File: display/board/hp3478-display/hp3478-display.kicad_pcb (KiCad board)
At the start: 2 copper layers, 130.2 x 30.2 mm, 4 parts, among them U1 PIC16F152xx-x_MP, U2 PIC16F152xx-x_PT

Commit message: Clean up DNP alternate footprint for PIC.
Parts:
- U1: value PIC16F152xx-x_MP -> PIC16F15274-I/MP
- U2: value PIC16F152xx-x_PT -> DNP
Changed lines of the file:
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@@
       (effects (font (size 1 1) (thickness 0.15)) (justify mirror))
     )
-    (fp_text value "PIC16F152xx-x_MP" (at 0 -3.82) (layer "B.Fab")
+    (fp_text value "PIC16F15274-I/MP" (at 0 -3.46875) (layer "B.Fab")
       (effects (font (size 1 1) (thickness 0.15)) (justify mirror))
     )
@@
     (property "Sheetfile" "hp3478-display.kicad_sch")
     (property "Sheetname" "")
-    (attr smd)
+    (property "exclude_from_bom" "")
+    (attr smd exclude_from_pos_files exclude_from_bom)
     (fp_text reference "U2" (at 0 7.45) (layer "B.SilkS") hide
       (effects (font (size 1 1) (thickness 0.15)) (justify mirror))
     )
-    (fp_text value "PIC16F152xx-x_PT" (at 0 -7.45) (layer "B.Fab")
+    (fp_text value "DNP" (at 0 -5.86875) (layer "B.Fab")
       (effects (font (size 1 1) (thickness 0.15)) (justify mirror))
     )
-    (fp_text user "${REFERENCE}" (at 0 0) (layer "B.Fab")
+    (fp_text user "${REFERENCE}" (at 0 4.13125) (layer "B.Fab")
       (effects (font (size 1 1) (thickness 0.15)) (justify mirror))
     )
@@
     )
   )
+  (group "" (id 6e3d8511-2586-4d9e-937b-9cb906607ab9)
+    (members
+      025682ff-41e6-48d6-90bc-8bc9fd15746c
+      0283738d-a418-4d7b-9e19-75ddbebbf050
+      06bb3c45-8662-472c-9176-38043edc8433
+      08d35165-bb31-44e7-9429-80a805175552
+      0a7519a3-5bb3-4d21-a876-66e5dc7dcb8d
+      0e3858fa-84b2-4190-b5dc-bcf350b77c61
+      101c4e56-94ee-448a-ae09-c0221e6f2d51
+      145eaf54-18e0-4b79-ba03-246c116e8f69
+      15e94442-0598-4a45-91b8-03f9b70ef5a3
+      16da12bf-2bc4-4194-ac8b-406fff70d2c3
+      1715dd60-2482-4e23-bc5e-3ba31d700b6f
+      1890f8e7-7f4d-463f-aff9-8671ab63580d
+      192e3839-8763-4b24-a518-5f7d4922fde5
+      1a80f237-de71-4763-80b9-d5010554198d
+      1c2f6f5d-567d-492e-90b1-d03751b21de6
+      1e06e057-1898-481f-9c88-3f5ebfa1e2fc
+      2028c6f6-e3dc-4ebc-aa0a-1362c4c273f7
+      21570638-80d9-4bae-a6cb-664d093151eb
+      2b77d2c8-977c-4773-b0bd-bde5d2c77fbc
+      2c354cff-9b07-49b8-ba75-7a25afc01f8d
+      2d844d1e-d000-4622-833b-a95b405f524e
+      2f1c99e4-9708-4779-a084-75db109c2f9c
+      2ffade97-e93c-4eaa-aabd-0226b2760495
+      345a010e-1fef-4904-91f1-bda43f6b94d0
+      34ce5afb-6d00-4f5b-96d5-474654a69470
+      37c44871-b5ca-4b38-aea3-1001c85da830
+      38ca2c34-44e4-4c73-9ecb-227d72018ede
+      4341d2f5-8f69-4bb4-89b6-485b5ccc8d94
+      48f444ee-de87-45be-b1f9-c20f4807963d
+      4db15927-cf44-4c49-9d54-4b4de7338f36
+      4eb2b707-4e67-4a79-8fa4-d5b3344d5c35
+      500f0cbe-700d-4821-bc8f-60759eeacedf
+      50c01e0b-0ee6-472b-9333-2379db306fa4
+      522140c8-51df-4cb0-80d1-d66afb59c4b8
+      530f5c91-5b5c-418c-b140-c1ccb08f07bb
+      54c19f1b-d006-4448-b08e-ed09ffd527e8
+      5bf72b43-8bfb-4f08-808e-46a6203671c8
+      5c8c4710-eed1-4240-878e-82181da0927d
+      5d507657-9866-419e-8279-080b059aeacd
+      5fac6f2c-6c6b-43ac-8c10-2c6f79dc15c3
+      60ea5389-bad7-4455-8498-5ab0665097fa
+      6580a8f1-f2ac-4be7-a759-ec333c75ea6f
+      67b13574-aef6-4e34-a5da-0348eaf75eff
+      683e9974-205a-4b76-84d5-c61235e00cdf
+      69365ee1-a7b1-43a5-8bad-a7db095cd6be
+      6c9397ea-235b-4ac5-ae90-efeac14b9162
+      7453fe99-c82a-4f4c-a960-c47a3c9abc0f
+      7adde682-d9cf-422d-8b9e-de7041a547f6
+      7b3583d4-0dcd-478a-9b70-53631796ddab
+      7b6b4f66-b8ef-4714-8f97-ea658228ba10
+      7d41948f-1b4b-4190-b337-199c340481b0
+      7d8cd68e-53e9-4780-a7b5-81e893b4aa44
+      7f1df24b-7067-45e9-8d0d-c04f6979bd1a
+      80d0327f-3161-4396-8853-6ca9f9deef36
+      81a76000-c235-495d-badf-e67f0e22323d
+      820e6614-d287-4578-9e51-4bf87f4b5f3c
+      82da71be-ab20-4e92-88af-ef4b842e5e4d
+      830267ac-4842-41eb-85aa-0bdeaf4c5da1
+      83f673a8-bf08-4bb5-a175-211bee14410e
+      83f68b42-ad69-4a08-a66f-0f1ad597741f
+      8976d532-97e7-4390-a5ee-ff48eeba3bc3
+      8d60349a-2b6c-4737-b106-263838d93f65
+      8f6142be-d54e-4d35-94e1-84ddd3d928f6
+      8f89d360-3807-4139-b3b1-4daea565fc2c
+      905a91b7-0f34-44b1-a98b-4c84c5d3c34e
+      93c134d8-7f21-4c40-8af1-1590fcb8ea30
+      9693fdcf-ada8-4fa4-902a-d7bcc7cb52e6
+      9ac5a0d4-3a85-4749-8d01-72dc6705821e
+      9e2301b9-18b8-493f-b249-928001b48921
+      9e802228-d3ca-450d-b5c2-e1e0526f26b0
+      9f70f681-a65d-4bfe-9163-cd3986453b6a
+      a2651f45-f233-4f7f-891c-41cf7e834619
+      a51fe366-2aae-45c2-aff7-f7f2d42fdd5c
+      acfde106-6ae1-4e80-ad04-4b11c2077337
+      ad824e11-9e43-4081-a47a-41356cebcfa1
+      ad8984a6-46a2-46bf-b149-408e18283ee8
+      ada6ff82-316c-40eb-ac3b-dee42e3d0fe0
+      adebfdb4-2d29-4cab-bad6-861392e3a973
+      aea8aee0-6918-4849-8951-0758496f3f77
+      af461771-7716-49bc-b6e1-a0cd07300201
+      b04d9136-b36c-4fd5-81bf-de6d48d242fd
+      b26fcc2b-fcf2-4a0d-bd8e-73c5c37df574
+      b2df7048-676f-4e9f-a937-85724a31c4da
+      b30e7e2d-9e8f-427b-b3de-40406137f752
+      b6e7d491-e815-46fe-a70b-e4e69542d985
+      b7a6e4bf-85bd-459a-8fae-cc24559051f6
+      bae503f5-737d-431e-ad8e-a732e1761b1b
+      bb3598e4-5f7d-4578-8eaf-08a0b2819f65
+      bba42b20-991e-4b6c-94ce-3b8912e848cc
+      bcafb699-73d4-48c1-8afc-c47ad2e6a319
+      bdda3f47-5fbc-4808-9d0b-3855365750ce
+      bf88b221-8c08-490d-8b1e-a107943edec0
+      c29e7f6c-6f8d-4f9c-973a-28026f9df1fb
+      c3786e45-6ed3-4e76-b21e-8784af082722
+      c50321ff-67fb-48a0-8459-fb8f04cc8330
+      c54809be-ddf7-4216-9bbe-d9ddd9bf1732
+      c5be51fb-343e-4a7f-b84b-60e8d21d866d
+      c9b8864b-ae54-495f-b221-7e6ec6c709a7
+      c9c9879b-016f-4837-ba81-059978bb2217
+      cae04ccc-ad7f-4d0e-bf06-386c7f95600e
+      cb28fc78-1799-48b6-b37d-a09e1e163ce1
+      cc302e30-08b3-40db-aea0-b70b83d47abb
+      cdaa8dca-88ad-4603-92ae-986a07685d3f
+      ce3cb9d7-7434-4c77-b49b-2743514ac2a5
+      d159ef80-b12c-4e4a-aac0-afe11b2aec94
+      d29bf029-20ec-498e-be4e-c731095d4b1c
+      d40135aa-c7cf-4a39-bd89-b1cadf488601
+      d9eac05d-343d-4b7c-87bd-ad8d3e738c26
+      df706935-3d1e-4b15-88b7-5f1ff1db0a64
+      e151b0ae-22d3-42f0-9fe4-0c76aee5e999
+      e36cef3a-00eb-428e-9a9e-5131e3191c38
+      e4e6bbe8-07a7-4fb3-a0ae-6e9f37464af7
+      e78e093a-b123-4233-8561-fb03e3faea37
+      e966890e-eb82-4482-bc0b-29c4cf736c9a
+      ea4d7fe6-ecb5-43fb-ae57-831410ea04c6
+      eb69106c-0a9f-4a6d-a725-65b06b5e0b18
+      eeacf475-42ac-4bbf-9966-97cc2bc637b5
+      ef24ac46-bc25-4a7c-aa47-53476bd5946b
+      f0499eab-fd69-47ae-bb8d-398502b2c35d
+      f38d1269-e152-43a2-a5fb-8e475846296c
+      f598361e-a767-4b5c-9b02-25b6d9b4113d
+      f7faf08c-a933-42b4-98d3-8e0e6d71c15a
+      fa3df00a-d72e-4478-93cc-9db95d7fea60
+      fbe8cd0b-c8ed-4616-b227-c8d81f4376d0
+      fd9cbe53-3183-4ef6-9c97-89df52042272
+      fe106c02-263d-4825-b67a-7fea6b9da52e
+    )
+  )

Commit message: Assign all pins.
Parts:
- added C1: 22u, Capacitor_SMD:C_1206_3216Metric, B.Cu at (82.9, 77.1)
- added C2: 100n, Capacitor_SMD:C_0603_1608Metric, B.Cu at (89.1, 59.1)
- added C3: 100n, Capacitor_SMD:C_0603_1608Metric, B.Cu at (99.3, 70.4)
- added J1: SFV10R-1ST, 0Local:Amphenol_SFV10R-1ST, B.Cu at (93.7, 77.1)
- added J2: DNP, Connector_PinHeader_2.54mm:PinHeader_1x06_P2.54mm_Vertical, B.Cu at (81.2, 58.5)
- added R10: R, Resistor_SMD:R_0603_1608Metric, B.Cu at (113.9, 55.9)
- added R11: R, Resistor_SMD:R_0603_1608Metric, B.Cu at (107.5, 56.8)
- added R12: R, Resistor_SMD:R_0603_1608Metric, B.Cu at (113.9, 57.7)
- added R13: R, Resistor_SMD:R_0603_1608Metric, B.Cu at (107.5, 58.5)
- added R14: R, Resistor_SMD:R_0603_1608Metric, B.Cu at (113.9, 63.0)
- added R15: R, Resistor_SMD:R_0603_1608Metric, B.Cu at (107.5, 63.9)
- added R16: R, Resistor_SMD:R_0603_1608Metric, B.Cu at (113.9, 64.8)
- added R17: R, Resistor_SMD:R_0603_1608Metric, B.Cu at (107.5, 65.7)
- added R18: R, Resistor_SMD:R_0603_1608Metric, B.Cu at (113.9, 59.4)
- added R19: R, Resistor_SMD:R_0603_1608Metric, B.Cu at (107.5, 60.3)
- added R20: R, Resistor_SMD:R_0603_1608Metric, B.Cu at (113.9, 61.2)
- added R21: R, Resistor_SMD:R_0603_1608Metric, B.Cu at (107.5, 62.1)
- added R22: R, Resistor_SMD:R_0603_1608Metric, B.Cu at (113.9, 66.5)
- added R23: R, Resistor_SMD:R_0603_1608Metric, B.Cu at (107.5, 67.4)
- added R24: R, Resistor_SMD:R_0603_1608Metric, B.Cu at (113.9, 68.3)
- added R25: R, Resistor_SMD:R_0603_1608Metric, B.Cu at (107.5, 69.2)
- added R26: R, Resistor_SMD:R_0603_1608Metric, B.Cu at (113.9, 70.1)
- moved U1 0.23 mm to (94.2, 64.8), turned to 135 degrees
- moved U2 0.23 mm to (94.2, 64.8), turned to 135 degrees
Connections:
- net Net-(U2-Pad1) renamed /HA7
- net Net-(U2-Pad10) renamed /K8
- net Net-(U2-Pad14) renamed /P1
- net Net-(U2-Pad15) renamed /SYNC
- net Net-(U2-Pad16) renamed /PGC/ISA
- net Net-(U2-Pad17) renamed /PGD/IWA
- net Net-(U2-Pad18) renamed /~{MCLR}
- net Net-(U2-Pad19) renamed /PWO
- net Net-(U2-Pad2) renamed /HA12
- net Net-(U2-Pad20) renamed /K0
- net Net-(U2-Pad21) renamed /K1
- net Net-(U2-Pad22) renamed /K2
- net Net-(U2-Pad23) renamed /K3
- net Net-(U2-Pad24) renamed /K4
- net Net-(U2-Pad25) renamed /K9
- net Net-(U2-Pad26) renamed /K10
- net Net-(U2-Pad27) renamed /K11
- net Net-(U2-Pad3) renamed /HA13
- net Net-(U2-Pad30) renamed /K6
- net Net-(U2-Pad31) renamed /K5
- net Net-(U2-Pad32) renamed /HA0
- net Net-(U2-Pad35) renamed /HA1
- net Net-(U2-Pad36) renamed /HA2
- net Net-(U2-Pad37) renamed /HA3
- net Net-(U2-Pad38) renamed /HA8
- net Net-(U2-Pad39) renamed /HA9
- net Net-(U2-Pad4) renamed /HA14
- net Net-(U2-Pad40) renamed /HA10
- net Net-(U2-Pad41) renamed /HA11
- net Net-(U2-Pad42) renamed /HA4
- net Net-(U2-Pad43) renamed /HA5
- net Net-(U2-Pad44) renamed /HA6
- net Net-(U2-Pad5) renamed /HA15
- net Net-(U2-Pad8) renamed /HA16
- net Net-(U2-Pad9) renamed /K7
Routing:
- net /A7: track 0.00 -> 94.0 mm
- net /A15: track 0.00 -> 94.0 mm
- net /A13: track 0.00 -> 94.0 mm
- net /A1: track 0.00 -> 94.0 mm
- net /A9: track 0.00 -> 93.9 mm
- net /A5: track 0.00 -> 93.9 mm
- net /A3: track 0.00 -> 93.9 mm
- net /A11: track 0.00 -> 93.9 mm
- net /A4: track 0.00 -> 87.7 mm
- net /A6: track 0.00 -> 87.6 mm
- net /A2: track 0.00 -> 87.6 mm
- net /A16: track 0.00 -> 87.6 mm
- net /A14: track 0.00 -> 87.6 mm
- net /A12: track 0.00 -> 87.6 mm
- net /A0: track 0.00 -> 87.6 mm
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
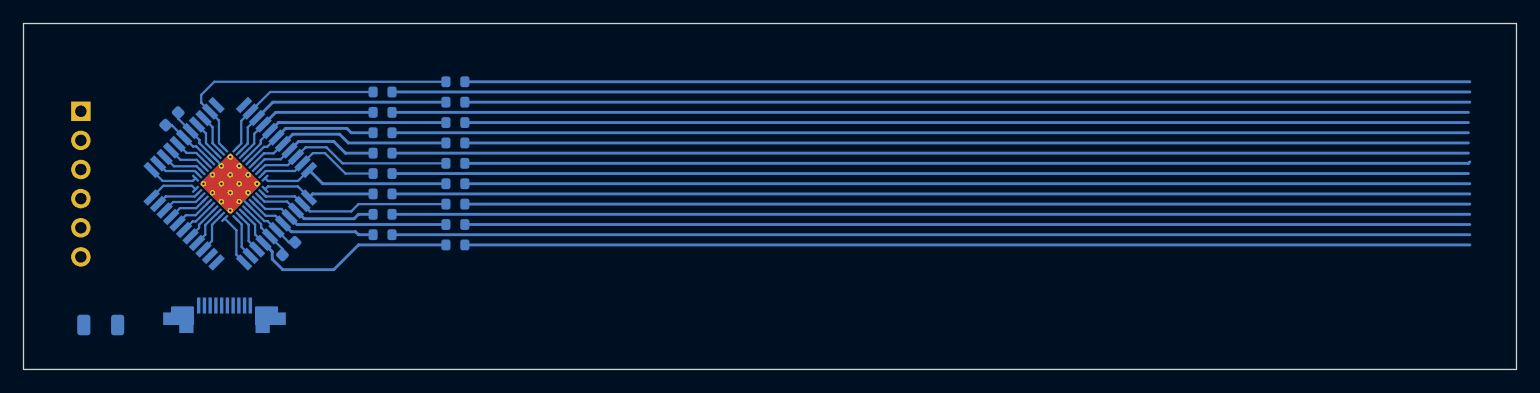
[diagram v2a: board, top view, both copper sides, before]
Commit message: Add digits to board.
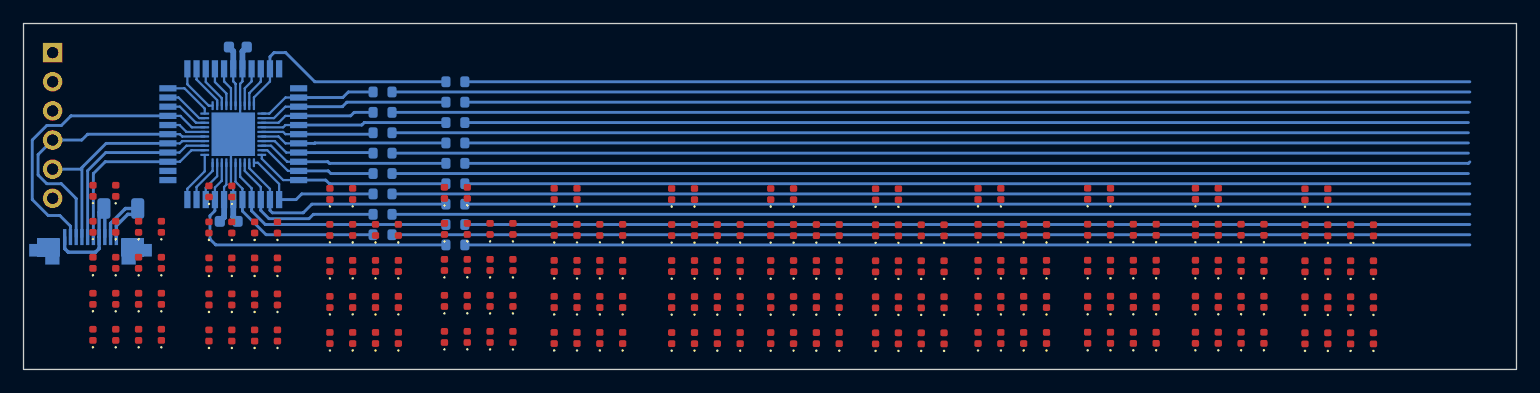
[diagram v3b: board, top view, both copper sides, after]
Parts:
- added D1001: LED, LED_SMD:LED_0402_1005Metric, F.Cu at (159.4, 78.2)
- added D1002: LED, LED_SMD:LED_0402_1005Metric, F.Cu at (161.4, 78.2)
- added D1003: LED, LED_SMD:LED_0402_1005Metric, F.Cu at (161.4, 65.7)
- added D1004: LED, LED_SMD:LED_0402_1005Metric, F.Cu at (159.4, 65.7)
- added D1005: LED, LED_SMD:LED_0402_1005Metric, F.Cu at (165.4, 78.2)
- added D1006: LED, LED_SMD:LED_0402_1005Metric, F.Cu at (161.4, 71.9)
- added D1007: LED, LED_SMD:LED_0402_1005Metric, F.Cu at (159.4, 68.8)
- added D1008: LED, LED_SMD:LED_0402_1005Metric, F.Cu at (163.4, 68.8)
- added D1009: LED, LED_SMD:LED_0402_1005Metric, F.Cu at (161.4, 75.1)
- added D1010: LED, LED_SMD:LED_0402_1005Metric, F.Cu at (165.4, 71.9)
- added D1011: LED, LED_SMD:LED_0402_1005Metric, F.Cu at (163.4, 75.1)
- added D1012: LED, LED_SMD:LED_0402_1005Metric, F.Cu at (165.4, 75.1)
- added D1013: LED, LED_SMD:LED_0402_1005Metric, F.Cu at (161.4, 68.8)
- added D1014: LED, LED_SMD:LED_0402_1005Metric, F.Cu at (163.4, 71.9)
- added D1015: LED, LED_SMD:LED_0402_1005Metric, F.Cu at (163.4, 78.2)
- added D1016: LED, LED_SMD:LED_0402_1005Metric, F.Cu at (159.4, 75.1)
- added D1017: LED, LED_SMD:LED_0402_1005Metric, F.Cu at (159.4, 71.9)
- added D1018: LED, LED_SMD:LED_0402_1005Metric, F.Cu at (165.4, 68.8)
- added D1101: LED, LED_SMD:LED_0402_1005Metric, F.Cu at (169.0, 78.2)
- added D1102: LED, LED_SMD:LED_0402_1005Metric, F.Cu at (171.0, 78.2)
- added D1103: LED, LED_SMD:LED_0402_1005Metric, F.Cu at (171.0, 65.6)
- added D1104: LED, LED_SMD:LED_0402_1005Metric, F.Cu at (169.0, 65.6)
- added D1105: LED, LED_SMD:LED_0402_1005Metric, F.Cu at (175.0, 78.2)
- added D1106: LED, LED_SMD:LED_0402_1005Metric, F.Cu at (171.0, 71.9)
- added D1107: LED, LED_SMD:LED_0402_1005Metric, F.Cu at (169.0, 68.8)
- added D1108: LED, LED_SMD:LED_0402_1005Metric, F.Cu at (173.0, 68.8)
- added D1109: LED, LED_SMD:LED_0402_1005Metric, F.Cu at (171.0, 75.1)
- added D1110: LED, LED_SMD:LED_0402_1005Metric, F.Cu at (175.0, 71.9)
- added D1111: LED, LED_SMD:LED_0402_1005Metric, F.Cu at (173.0, 75.1)
- added D1112: LED, LED_SMD:LED_0402_1005Metric, F.Cu at (175.0, 75.1)
- added D1113: LED, LED_SMD:LED_0402_1005Metric, F.Cu at (171.0, 68.8)
- added D1114: LED, LED_SMD:LED_0402_1005Metric, F.Cu at (173.0, 71.9)
- added D1115: LED, LED_SMD:LED_0402_1005Metric, F.Cu at (173.0, 78.2)
- added D1116: LED, LED_SMD:LED_0402_1005Metric, F.Cu at (169.0, 75.1)
- added D1117: LED, LED_SMD:LED_0402_1005Metric, F.Cu at (169.0, 71.9)
- added D1118: LED, LED_SMD:LED_0402_1005Metric, F.Cu at (175.0, 68.8)
- added D1201: LED, LED_SMD:LED_0402_1005Metric, F.Cu at (178.4, 78.2)
- added D1202: LED, LED_SMD:LED_0402_1005Metric, F.Cu at (180.4, 78.2)
- added D1203: LED, LED_SMD:LED_0402_1005Metric, F.Cu at (180.4, 65.6)
- added D1204: LED, LED_SMD:LED_0402_1005Metric, F.Cu at (178.4, 65.6)
- added D1205: LED, LED_SMD:LED_0402_1005Metric, F.Cu at (184.4, 78.2)
- added D1206: LED, LED_SMD:LED_0402_1005Metric, F.Cu at (180.4, 71.9)
- added D1207: LED, LED_SMD:LED_0402_1005Metric, F.Cu at (178.4, 68.8)
- added D1208: LED, LED_SMD:LED_0402_1005Metric, F.Cu at (182.4, 68.8)
- added D1209: LED, LED_SMD:LED_0402_1005Metric, F.Cu at (180.4, 75.1)
- added D1210: LED, LED_SMD:LED_0402_1005Metric, F.Cu at (184.4, 71.9)
- added D1211: LED, LED_SMD:LED_0402_1005Metric, F.Cu at (182.4, 75.1)
- added D1212: LED, LED_SMD:LED_0402_1005Metric, F.Cu at (184.4, 75.1)
- added D1213: LED, LED_SMD:LED_0402_1005Metric, F.Cu at (180.4, 68.8)
- added D1214: LED, LED_SMD:LED_0402_1005Metric, F.Cu at (182.4, 71.9)
- added D1215: LED, LED_SMD:LED_0402_1005Metric, F.Cu at (182.4, 78.2)
- added D1216: LED, LED_SMD:LED_0402_1005Metric, F.Cu at (178.4, 75.1)
- added D1217: LED, LED_SMD:LED_0402_1005Metric, F.Cu at (178.4, 71.9)
- added D1218: LED, LED_SMD:LED_0402_1005Metric, F.Cu at (184.4, 68.8)
- added D1301: LED, LED_SMD:LED_0402_1005Metric, F.Cu at (187.9, 78.3)
- added D1302: LED, LED_SMD:LED_0402_1005Metric, F.Cu at (189.9, 78.3)
- added D1303: LED, LED_SMD:LED_0402_1005Metric, F.Cu at (189.9, 65.7)
- added D1304: LED, LED_SMD:LED_0402_1005Metric, F.Cu at (187.9, 65.7)
- added D1305: LED, LED_SMD:LED_0402_1005Metric, F.Cu at (193.9, 78.3)
- added D1306: LED, LED_SMD:LED_0402_1005Metric, F.Cu at (189.9, 72.0)
- added D1307: LED, LED_SMD:LED_0402_1005Metric, F.Cu at (187.9, 68.8)
- added D1308: LED, LED_SMD:LED_0402_1005Metric, F.Cu at (191.9, 68.8)
- added D1309: LED, LED_SMD:LED_0402_1005Metric, F.Cu at (189.9, 75.1)
- added D1310: LED, LED_SMD:LED_0402_1005Metric, F.Cu at (193.9, 72.0)
- added D1311: LED, LED_SMD:LED_0402_1005Metric, F.Cu at (191.9, 75.1)
- added D1312: LED, LED_SMD:LED_0402_1005Metric, F.Cu at (193.9, 75.1)
- added D1313: LED, LED_SMD:LED_0402_1005Metric, F.Cu at (189.9, 68.8)
- added D1314: LED, LED_SMD:LED_0402_1005Metric, F.Cu at (191.9, 72.0)
- added D1315: LED, LED_SMD:LED_0402_1005Metric, F.Cu at (191.9, 78.3)
- added D1316: LED, LED_SMD:LED_0402_1005Metric, F.Cu at (187.9, 75.1)
- added D1317: LED, LED_SMD:LED_0402_1005Metric, F.Cu at (187.9, 72.0)
- added D1318: LED, LED_SMD:LED_0402_1005Metric, F.Cu at (193.9, 68.8)
- added D201: LED, LED_SMD:LED_0402_1005Metric, F.Cu at (82.3, 77.9)
- added D202: LED, LED_SMD:LED_0402_1005Metric, F.Cu at (84.2, 77.9)
- added D203: LED, LED_SMD:LED_0402_1005Metric, F.Cu at (84.2, 65.4)
- added D204: LED, LED_SMD:LED_0402_1005Metric, F.Cu at (82.3, 65.4)
- added D205: LED, LED_SMD:LED_0402_1005Metric, F.Cu at (88.2, 77.9)
- added D206: LED, LED_SMD:LED_0402_1005Metric, F.Cu at (84.2, 71.7)
- added D207: LED, LED_SMD:LED_0402_1005Metric, F.Cu at (82.3, 68.5)
- added D208: LED, LED_SMD:LED_0402_1005Metric, F.Cu at (86.2, 68.5)
- added D209: LED, LED_SMD:LED_0402_1005Metric, F.Cu at (84.2, 74.8)
- added D210: LED, LED_SMD:LED_0402_1005Metric, F.Cu at (88.2, 71.7)
- added D211: LED, LED_SMD:LED_0402_1005Metric, F.Cu at (86.2, 74.8)
- added D212: LED, LED_SMD:LED_0402_1005Metric, F.Cu at (88.2, 74.8)
- added D213: LED, LED_SMD:LED_0402_1005Metric, F.Cu at (84.2, 68.5)
- added D214: LED, LED_SMD:LED_0402_1005Metric, F.Cu at (86.2, 71.7)
- added D215: LED, LED_SMD:LED_0402_1005Metric, F.Cu at (86.2, 77.9)
- added D216: LED, LED_SMD:LED_0402_1005Metric, F.Cu at (82.3, 74.8)
- added D217: LED, LED_SMD:LED_0402_1005Metric, F.Cu at (82.3, 71.7)
- added D218: LED, LED_SMD:LED_0402_1005Metric, F.Cu at (88.2, 68.5)
- added D301: LED, LED_SMD:LED_0402_1005Metric, F.Cu at (92.4, 78.0)
- added D302: LED, LED_SMD:LED_0402_1005Metric, F.Cu at (94.4, 78.0)
- added D303: LED, LED_SMD:LED_0402_1005Metric, F.Cu at (94.4, 65.4)
- added D304: LED, LED_SMD:LED_0402_1005Metric, F.Cu at (92.4, 65.4)
- added D305: LED, LED_SMD:LED_0402_1005Metric, F.Cu at (98.3, 78.0)
- added D306: LED, LED_SMD:LED_0402_1005Metric, F.Cu at (94.4, 71.7)
- added D307: LED, LED_SMD:LED_0402_1005Metric, F.Cu at (92.4, 68.6)
- added D308: LED, LED_SMD:LED_0402_1005Metric, F.Cu at (96.4, 68.6)
- added D309: LED, LED_SMD:LED_0402_1005Metric, F.Cu at (94.4, 74.9)
- added D310: LED, LED_SMD:LED_0402_1005Metric, F.Cu at (98.3, 71.7)
- added D311: LED, LED_SMD:LED_0402_1005Metric, F.Cu at (96.4, 74.9)
- added D312: LED, LED_SMD:LED_0402_1005Metric, F.Cu at (98.3, 74.9)
- added D313: LED, LED_SMD:LED_0402_1005Metric, F.Cu at (94.4, 68.6)
- added D314: LED, LED_SMD:LED_0402_1005Metric, F.Cu at (96.4, 71.7)
- added D315: LED, LED_SMD:LED_0402_1005Metric, F.Cu at (96.4, 78.0)
- added D316: LED, LED_SMD:LED_0402_1005Metric, F.Cu at (92.4, 74.9)
- added D317: LED, LED_SMD:LED_0402_1005Metric, F.Cu at (92.4, 71.7)
- added D318: LED, LED_SMD:LED_0402_1005Metric, F.Cu at (98.3, 68.6)
- added D401: LED, LED_SMD:LED_0402_1005Metric, F.Cu at (102.9, 78.2)
- added D402: LED, LED_SMD:LED_0402_1005Metric, F.Cu at (104.9, 78.2)
- added D403: LED, LED_SMD:LED_0402_1005Metric, F.Cu at (104.9, 65.7)
- added D404: LED, LED_SMD:LED_0402_1005Metric, F.Cu at (102.9, 65.7)
- added D405: LED, LED_SMD:LED_0402_1005Metric, F.Cu at (108.9, 78.2)
- added D406: LED, LED_SMD:LED_0402_1005Metric, F.Cu at (104.9, 71.9)
- added D407: LED, LED_SMD:LED_0402_1005Metric, F.Cu at (102.9, 68.8)
- added D408: LED, LED_SMD:LED_0402_1005Metric, F.Cu at (106.9, 68.8)
- added D409: LED, LED_SMD:LED_0402_1005Metric, F.Cu at (104.9, 75.1)
- added D410: LED, LED_SMD:LED_0402_1005Metric, F.Cu at (108.9, 71.9)
- added D411: LED, LED_SMD:LED_0402_1005Metric, F.Cu at (106.9, 75.1)
- added D412: LED, LED_SMD:LED_0402_1005Metric, F.Cu at (108.9, 75.1)
- added D413: LED, LED_SMD:LED_0402_1005Metric, F.Cu at (104.9, 68.8)
- added D414: LED, LED_SMD:LED_0402_1005Metric, F.Cu at (106.9, 71.9)
- added D415: LED, LED_SMD:LED_0402_1005Metric, F.Cu at (106.9, 78.2)
- added D416: LED, LED_SMD:LED_0402_1005Metric, F.Cu at (102.9, 75.1)
- added D417: LED, LED_SMD:LED_0402_1005Metric, F.Cu at (102.9, 71.9)
- added D418: LED, LED_SMD:LED_0402_1005Metric, F.Cu at (108.9, 68.8)
- added D501: LED, LED_SMD:LED_0402_1005Metric, F.Cu at (112.9, 78.1)
- added D502: LED, LED_SMD:LED_0402_1005Metric, F.Cu at (114.9, 78.1)
- added D503: LED, LED_SMD:LED_0402_1005Metric, F.Cu at (114.9, 65.6)
- added D504: LED, LED_SMD:LED_0402_1005Metric, F.Cu at (112.9, 65.6)
- added D505: LED, LED_SMD:LED_0402_1005Metric, F.Cu at (118.9, 78.1)
- added D506: LED, LED_SMD:LED_0402_1005Metric, F.Cu at (114.9, 71.8)
- added D507: LED, LED_SMD:LED_0402_1005Metric, F.Cu at (112.9, 68.7)
- added D508: LED, LED_SMD:LED_0402_1005Metric, F.Cu at (116.9, 68.7)
- added D509: LED, LED_SMD:LED_0402_1005Metric, F.Cu at (114.9, 75.0)
- added D510: LED, LED_SMD:LED_0402_1005Metric, F.Cu at (118.9, 71.8)
- added D511: LED, LED_SMD:LED_0402_1005Metric, F.Cu at (116.9, 75.0)
- added D512: LED, LED_SMD:LED_0402_1005Metric, F.Cu at (118.9, 75.0)
- added D513: LED, LED_SMD:LED_0402_1005Metric, F.Cu at (114.9, 68.7)
- added D514: LED, LED_SMD:LED_0402_1005Metric, F.Cu at (116.9, 71.8)
- added D515: LED, LED_SMD:LED_0402_1005Metric, F.Cu at (116.9, 78.1)
- added D516: LED, LED_SMD:LED_0402_1005Metric, F.Cu at (112.9, 75.0)
- added D517: LED, LED_SMD:LED_0402_1005Metric, F.Cu at (112.9, 71.8)
- added D518: LED, LED_SMD:LED_0402_1005Metric, F.Cu at (118.9, 68.7)
- added D601: LED, LED_SMD:LED_0402_1005Metric, F.Cu at (122.5, 78.2)
- added D602: LED, LED_SMD:LED_0402_1005Metric, F.Cu at (124.5, 78.2)
- added D603: LED, LED_SMD:LED_0402_1005Metric, F.Cu at (124.5, 65.7)
- added D604: LED, LED_SMD:LED_0402_1005Metric, F.Cu at (122.5, 65.7)
- added D605: LED, LED_SMD:LED_0402_1005Metric, F.Cu at (128.4, 78.2)
- added D606: LED, LED_SMD:LED_0402_1005Metric, F.Cu at (124.5, 71.9)
- added D607: LED, LED_SMD:LED_0402_1005Metric, F.Cu at (122.5, 68.8)
- added D608: LED, LED_SMD:LED_0402_1005Metric, F.Cu at (126.5, 68.8)
- added D609: LED, LED_SMD:LED_0402_1005Metric, F.Cu at (124.5, 75.1)
- added D610: LED, LED_SMD:LED_0402_1005Metric, F.Cu at (128.4, 71.9)
- added D611: LED, LED_SMD:LED_0402_1005Metric, F.Cu at (126.5, 75.1)
- added D612: LED, LED_SMD:LED_0402_1005Metric, F.Cu at (128.4, 75.1)
- added D613: LED, LED_SMD:LED_0402_1005Metric, F.Cu at (124.5, 68.8)
- added D614: LED, LED_SMD:LED_0402_1005Metric, F.Cu at (126.5, 71.9)
- added D615: LED, LED_SMD:LED_0402_1005Metric, F.Cu at (126.5, 78.2)
- added D616: LED, LED_SMD:LED_0402_1005Metric, F.Cu at (122.5, 75.1)
- added D617: LED, LED_SMD:LED_0402_1005Metric, F.Cu at (122.5, 71.9)
- added D618: LED, LED_SMD:LED_0402_1005Metric, F.Cu at (128.4, 68.8)
- added D701: LED, LED_SMD:LED_0402_1005Metric, F.Cu at (132.7, 78.2)
- added D702: LED, LED_SMD:LED_0402_1005Metric, F.Cu at (134.7, 78.2)
- added D703: LED, LED_SMD:LED_0402_1005Metric, F.Cu at (134.7, 65.7)
- added D704: LED, LED_SMD:LED_0402_1005Metric, F.Cu at (132.7, 65.7)
- added D705: LED, LED_SMD:LED_0402_1005Metric, F.Cu at (138.7, 78.2)
- added D706: LED, LED_SMD:LED_0402_1005Metric, F.Cu at (134.7, 72.0)
- added D707: LED, LED_SMD:LED_0402_1005Metric, F.Cu at (132.7, 68.8)
- added D708: LED, LED_SMD:LED_0402_1005Metric, F.Cu at (136.7, 68.8)
- added D709: LED, LED_SMD:LED_0402_1005Metric, F.Cu at (134.7, 75.1)
- added D710: LED, LED_SMD:LED_0402_1005Metric, F.Cu at (138.7, 72.0)
- added D711: LED, LED_SMD:LED_0402_1005Metric, F.Cu at (136.7, 75.1)
- added D712: LED, LED_SMD:LED_0402_1005Metric, F.Cu at (138.7, 75.1)
- added D713: LED, LED_SMD:LED_0402_1005Metric, F.Cu at (134.7, 68.8)
- added D714: LED, LED_SMD:LED_0402_1005Metric, F.Cu at (136.7, 72.0)
- added D715: LED, LED_SMD:LED_0402_1005Metric, F.Cu at (136.7, 78.2)
- added D716: LED, LED_SMD:LED_0402_1005Metric, F.Cu at (132.7, 75.1)
- added D717: LED, LED_SMD:LED_0402_1005Metric, F.Cu at (132.7, 72.0)
- added D718: LED, LED_SMD:LED_0402_1005Metric, F.Cu at (138.7, 68.8)
- added D801: LED, LED_SMD:LED_0402_1005Metric, F.Cu at (141.3, 78.2)
- added D802: LED, LED_SMD:LED_0402_1005Metric, F.Cu at (143.3, 78.2)
- added D803: LED, LED_SMD:LED_0402_1005Metric, F.Cu at (143.3, 65.7)
- added D804: LED, LED_SMD:LED_0402_1005Metric, F.Cu at (141.3, 65.7)
- added D805: LED, LED_SMD:LED_0402_1005Metric, F.Cu at (147.3, 78.2)
- added D806: LED, LED_SMD:LED_0402_1005Metric, F.Cu at (143.3, 72.0)
- added D807: LED, LED_SMD:LED_0402_1005Metric, F.Cu at (141.3, 68.8)
- added D808: LED, LED_SMD:LED_0402_1005Metric, F.Cu at (145.3, 68.8)
- added D809: LED, LED_SMD:LED_0402_1005Metric, F.Cu at (143.3, 75.1)
- added D810: LED, LED_SMD:LED_0402_1005Metric, F.Cu at (147.3, 72.0)
- added D811: LED, LED_SMD:LED_0402_1005Metric, F.Cu at (145.3, 75.1)
- added D812: LED, LED_SMD:LED_0402_1005Metric, F.Cu at (147.3, 75.1)
- added D813: LED, LED_SMD:LED_0402_1005Metric, F.Cu at (143.3, 68.8)
- added D814: LED, LED_SMD:LED_0402_1005Metric, F.Cu at (145.3, 72.0)
- added D815: LED, LED_SMD:LED_0402_1005Metric, F.Cu at (145.3, 78.2)
- added D816: LED, LED_SMD:LED_0402_1005Metric, F.Cu at (141.3, 75.1)
- added D817: LED, LED_SMD:LED_0402_1005Metric, F.Cu at (141.3, 72.0)
- added D818: LED, LED_SMD:LED_0402_1005Metric, F.Cu at (147.3, 68.8)
- added D901: LED, LED_SMD:LED_0402_1005Metric, F.Cu at (150.5, 78.3)
- added D902: LED, LED_SMD:LED_0402_1005Metric, F.Cu at (152.5, 78.3)
- added D903: LED, LED_SMD:LED_0402_1005Metric, F.Cu at (152.5, 65.7)
- added D904: LED, LED_SMD:LED_0402_1005Metric, F.Cu at (150.5, 65.7)
- added D905: LED, LED_SMD:LED_0402_1005Metric, F.Cu at (156.5, 78.3)
- added D906: LED, LED_SMD:LED_0402_1005Metric, F.Cu at (152.5, 72.0)
- added D907: LED, LED_SMD:LED_0402_1005Metric, F.Cu at (150.5, 68.8)
- added D908: LED, LED_SMD:LED_0402_1005Metric, F.Cu at (154.5, 68.8)
- added D909: LED, LED_SMD:LED_0402_1005Metric, F.Cu at (152.5, 75.1)
- added D910: LED, LED_SMD:LED_0402_1005Metric, F.Cu at (156.5, 72.0)
- added D911: LED, LED_SMD:LED_0402_1005Metric, F.Cu at (154.5, 75.1)
- added D912: LED, LED_SMD:LED_0402_1005Metric, F.Cu at (156.5, 75.1)
- added D913: LED, LED_SMD:LED_0402_1005Metric, F.Cu at (152.5, 68.8)
- added D914: LED, LED_SMD:LED_0402_1005Metric, F.Cu at (154.5, 72.0)
- added D915: LED, LED_SMD:LED_0402_1005Metric, F.Cu at (154.5, 78.3)
- added D916: LED, LED_SMD:LED_0402_1005Metric, F.Cu at (150.5, 75.1)
- added D917: LED, LED_SMD:LED_0402_1005Metric, F.Cu at (150.5, 72.0)
- added D918: LED, LED_SMD:LED_0402_1005Metric, F.Cu at (156.5, 68.8)
- U1: footprint Package_DFN_QFN:QFN-40-1EP_5x5mm_P0.4mm_EP3.8x3.8mm_ThermalVias -> Package_DFN_QFN:QFN-40-1EP_5x5mm_P0.4mm_EP3.8x3.8mm
- moved J1 13.1 mm to (82.0, 71.1)
- moved C1 10.3 mm to (84.7, 66.9)
- moved C2 8.50 mm to (94.9, 52.9), turned to 0 degrees
- moved C3 5.75 mm to (94.1, 68.1), turned to 0 degrees
- moved J2 5.67 mm to (78.7, 53.3)
- moved U1 4.33 mm to (94.5, 60.5), turned to 90 degrees
- moved U2 4.33 mm to (94.5, 60.5), turned to 90 degrees
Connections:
- J1 pad 5: unconnected-(J1-Pad5) -> /P1
- J1 pad 6: unconnected-(J1-Pad6) -> /SYNC
- J1 pad 7: unconnected-(J1-Pad7) -> /PGC/ISA
- J1 pad 8: unconnected-(J1-Pad8) -> /PGD/IWA
- J1 pad 9: unconnected-(J1-Pad9) -> /PWO
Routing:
- net /PWO: track 3.63 -> 26.8 mm
- net /PGD/IWA: track 3.30 -> 24.7 mm
- net /PGC/ISA: track 3.30 -> 20.3 mm
- net /SYNC: track 3.46 -> 16.9 mm
- net /P1: track 3.63 -> 16.1 mm
- net GND: track 14.1 -> 24.6 mm
- net +5V: track 10.7 -> 18.4 mm
- net /HA16: track 21.6 -> 27.9 mm
- net /HA0: track 27.4 -> 21.4 mm
- net /HA15: track 11.7 -> 16.7 mm
- net /HA1: track 15.2 -> 10.5 mm
- net /HA14: track 17.5 -> 22.0 mm
- net /HA2: track 20.7 -> 16.6 mm
- net /HA13: track 11.0 -> 15.0 mm
- net /HA12: track 17.0 -> 20.7 mm
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
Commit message: Reorganize schematic.
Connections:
- D1017 pad 1: /K8 -> Net-(D1018-Pad2)
- D1018 pad 2: /A16 -> Net-(D1018-Pad2)
- D1117 pad 1: /K9 -> Net-(D1118-Pad2)
- D1118 pad 2: /A16 -> Net-(D1118-Pad2)
- D1217 pad 1: /K10 -> Net-(D1218-Pad2)
- D1218 pad 2: /A16 -> Net-(D1218-Pad2)
- D1317 pad 1: /K11 -> Net-(D1318-Pad2)
- D1318 pad 2: /A16 -> Net-(D1318-Pad2)
- D217 pad 1: /K0 -> Net-(D218-Pad2)
- D218 pad 2: /A16 -> Net-(D218-Pad2)
- D317 pad 1: /K1 -> Net-(D318-Pad2)
- D318 pad 2: /A16 -> Net-(D318-Pad2)
- D417 pad 1: /K2 -> Net-(D418-Pad2)
- D418 pad 2: /A16 -> Net-(D418-Pad2)
- D517 pad 1: /K3 -> Net-(D518-Pad2)
- D518 pad 2: /A16 -> Net-(D518-Pad2)
- D617 pad 1: /K4 -> Net-(D618-Pad2)
- D618 pad 2: /A16 -> Net-(D618-Pad2)
- D717 pad 1: /K5 -> Net-(D718-Pad2)
- D718 pad 2: /A16 -> Net-(D718-Pad2)
- D817 pad 1: /K6 -> Net-(D818-Pad2)
- D818 pad 2: /A16 -> Net-(D818-Pad2)
- D917 pad 1: /K7 -> Net-(D918-Pad2)
- D918 pad 2: /A16 -> Net-(D918-Pad2)
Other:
- board size 130.2 x 30.2 mm -> 130.2 x 29.8 mm
